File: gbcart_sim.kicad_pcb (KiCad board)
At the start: 2 copper layers, 134.1 x 70.1 mm, 27 parts, among them J1 Micro_SD_Card, J2 Conn_02x17_Odd_Even, J3 Conn_01x32, Q1 BC847, SW1 SW_Push, U1 ESP32-S3-DevKitC, U2 74lxc125, U3 74HC138, U4 74HCT1G125, U5 74HC259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

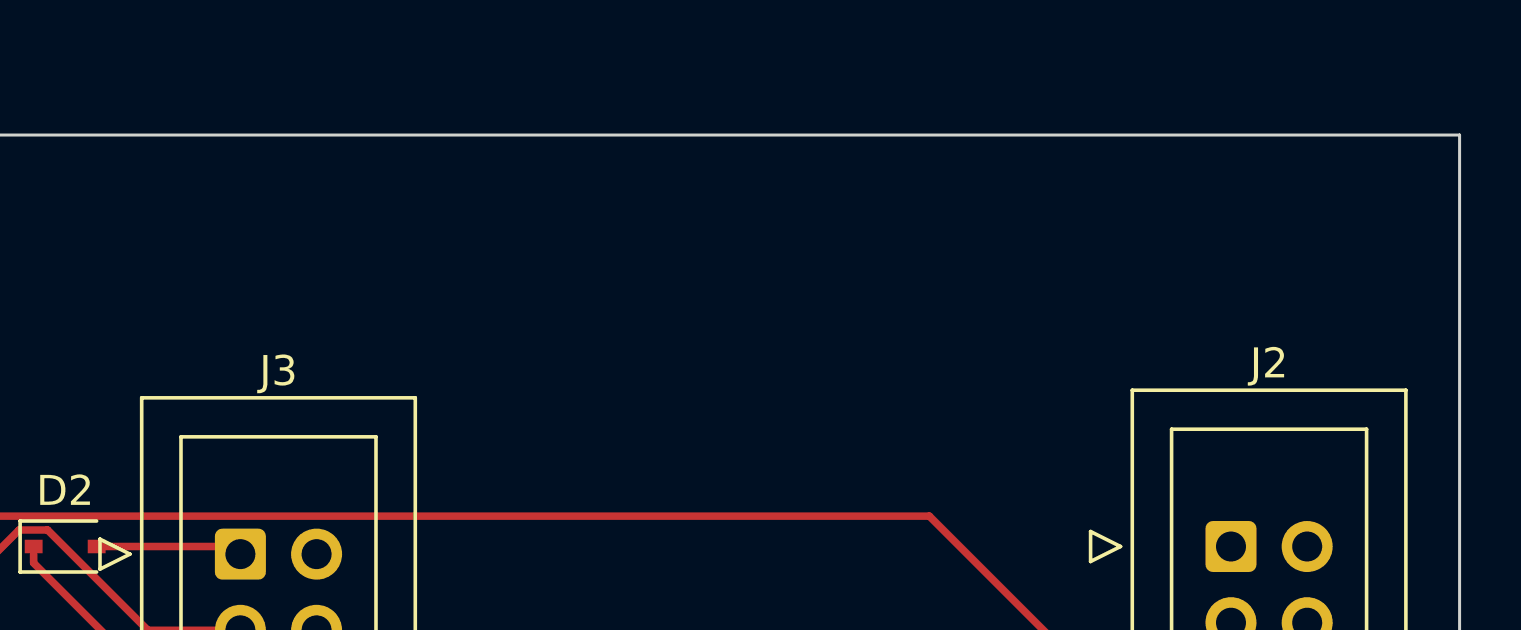
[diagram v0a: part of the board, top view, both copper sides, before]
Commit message: Move connector + add silkscren names
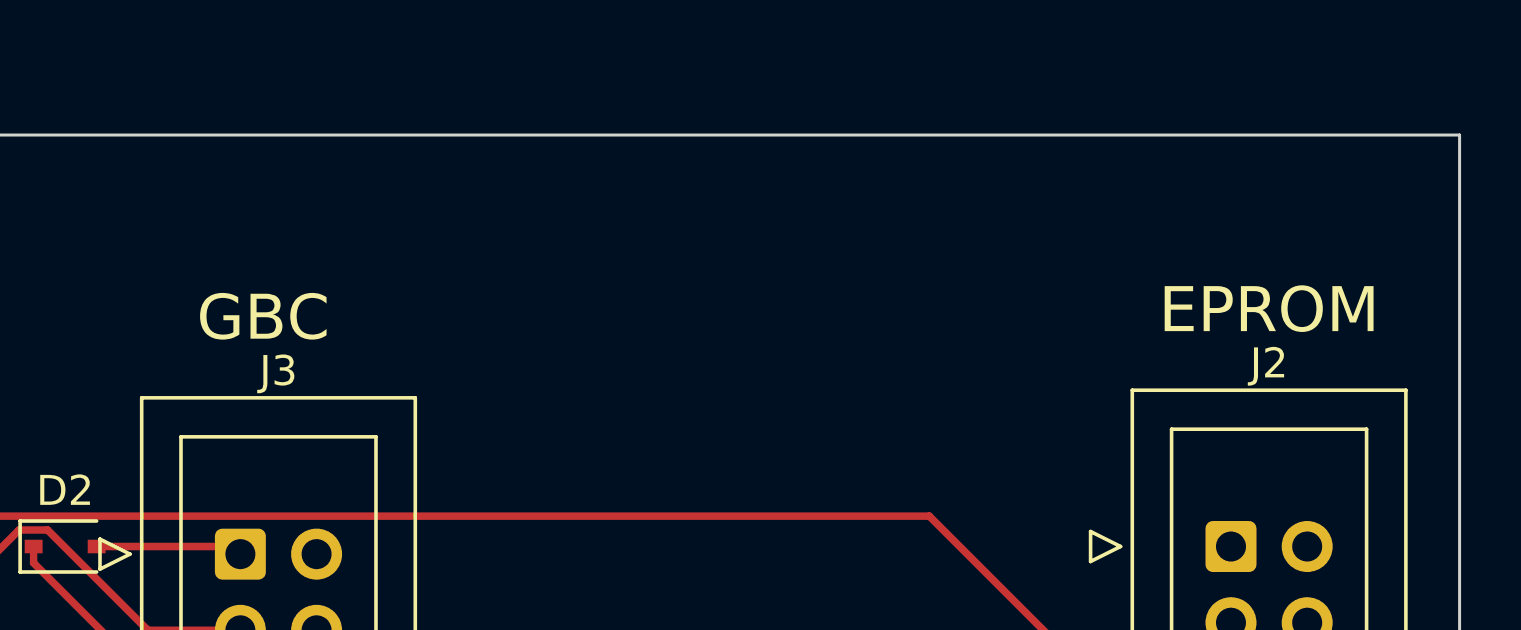
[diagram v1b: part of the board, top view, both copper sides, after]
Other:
- board text added: "EPROM"
- board text added: "GBC"
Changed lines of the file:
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@@
     (effects (font (size 1.5 1.5) (thickness 0.3)) (justify mirror))
+  )
+  (gr_text "GBC" (at 124.714 85.852) (layer "F.SilkS")
+    (effects (font (size 1.5 1.5) (thickness 0.3)))
+  )
+  (gr_text "EPROM" (at 158.242 85.598) (layer "F.SilkS")
+    (effects (font (size 1.5 1.5) (thickness 0.3)))
   )
   (segment (start 117.3385 131.8734) (end 123.9046 131.8734) (width 0.25) (layer "F.Cu") (net 1))

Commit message: Fix board
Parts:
- added U7: 74HCT1G125, Package_TO_SOT_SMD:SOT-353_SC-70-5_Handsoldering, F.Cu at (97.1, 119.2)
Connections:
- U1 pad 37: unconnected-(U1-Pad37) -> Net-(U1-Pad37)
- U5 pad 15: /GB.~{RST} -> Net-(U5-Pad15)
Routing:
- net /GB.~{RST}: track 139.7 -> 103.7 mm
- net Net-(U1-Pad37): track 0.00 -> 32.1 mm, vias 0 -> 1
- net GND: track 372.4 -> 382.0 mm, vias 1 -> 3
- net Net-(U5-Pad15): track 0.00 -> 8.70 mm
- net +5V: track 163.4 -> 165.9 mm

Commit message: Generate production files
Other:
- board text added: "v2.0"
- board text removed: "DEV"
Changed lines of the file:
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@@
       (outputformat 1)
       (mirror false)
-      (drillshape 1)
+      (drillshape 0)
       (scaleselection 1)
-      (outputdirectory "")
+      (outputdirectory "gbusbcart_sim/gerbers/")
     )
   )
@@
     (fp_line (start -3.65 2.15) (end 3.65 2.15) (layer "F.Fab") (width 0.1))
     (fp_line (start -2.65 -2.15) (end -3.65 -1.15) (layer "F.Fab") (width 0.1))
-    (pad "1" smd roundrect (at -3.1125 0) (size 2.075 2.55) (layers "F.Cu" "F.Paste" "F.Mask") (roundrect_rratio 0.120482)
+    (pad "1" smd roundrect (at -3.1125 0) (size 2.075 2.55) (layers "F.Cu" "F.Paste" "F.Mask") (roundrect_rratio 0.1204819277)
       (net 92 "/GPIO41") (pintype "passive"))
-    (pad "2" smd roundrect (at 3.1125 0) (size 2.075 2.55) (layers "F.Cu" "F.Paste" "F.Mask") (roundrect_rratio 0.120482)
+    (pad "2" smd roundrect (at 3.1125 0) (size 2.075 2.55) (layers "F.Cu" "F.Paste" "F.Mask") (roundrect_rratio 0.1204819277)
       (net 1 "/GB.AUDIO") (pintype "passive"))
     (model "${KICAD6_3DMODEL_DIR}/Capacitor_Tantalum_SMD.3dshapes/CP_EIA-7343-31_Kemet-D.wrl"
@@
     (fp_line (start 5.72 45.74) (end -3.18 45.74) (layer "F.Fab") (width 0.1))
     (fp_line (start 5.72 -5.1) (end 5.72 45.74) (layer "F.Fab") (width 0.1))
-    (pad "1" thru_hole roundrect (at 0 0) (size 1.7 1.7) (drill 1) (layers *.Cu *.Mask) (roundrect_rratio 0.147059)
+    (pad "1" thru_hole roundrect (at 0 0) (size 1.7 1.7) (drill 1) (layers *.Cu *.Mask) (roundrect_rratio 0.1470588235)
       (net 8 "Net-(D2-Pad2)") (pinfunction "Pin_1") (pintype "passive"))
     (pad "2" thru_hole circle (at 2.54 0) (size 1.7 1.7) (drill 1) (layers *.Cu *.Mask)
@@
     (fp_line (start 5.72 -5.1) (end 5.72 45.74) (layer "F.Fab") (width 0.1))
     (fp_line (start -1.98 18.27) (end -1.98 -3.91) (layer "F.Fab") (width 0.1))
-    (pad "1" thru_hole roundrect (at 0 0) (size 1.7 1.7) (drill 1) (layers *.Cu *.Mask) (roundrect_rratio 0.147059)
+    (pad "1" thru_hole roundrect (at 0 0) (size 1.7 1.7) (drill 1) (layers *.Cu *.Mask) (roundrect_rratio 0.1470588235)
       (net 87 "unconnected-(J2-Pad1)") (pinfunction "Pin_1") (pintype "passive"))
     (pad "2" thru_hole circle (at 2.54 0) (size 1.7 1.7) (drill 1) (layers *.Cu *.Mask)
@@
     (effects (font (size 1.5 1.5) (thickness 0.3)) (justify mirror))
   )
-  (gr_text "DEV" (at 99.568 89.662) (layer "B.Cu")
+  (gr_text "v2.0" (at 99.568 89.662) (layer "B.Cu")
     (effects (font (size 1.5 1.5) (thickness 0.3)) (justify mirror))
   )
